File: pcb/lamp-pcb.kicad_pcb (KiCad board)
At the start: 2 copper layers, 105.4 x 91.4 mm, 41 parts, among them IC1 ATMEGA328P, IC2 LM1117, IC3 TLC5973, J1 5V_OUT, J2 LED_CARD_BOTTOM, M2 Val**, P1 7-12V_IN, P2 AVR_ISP, P3 SERIAL, P4 LEDSTACK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

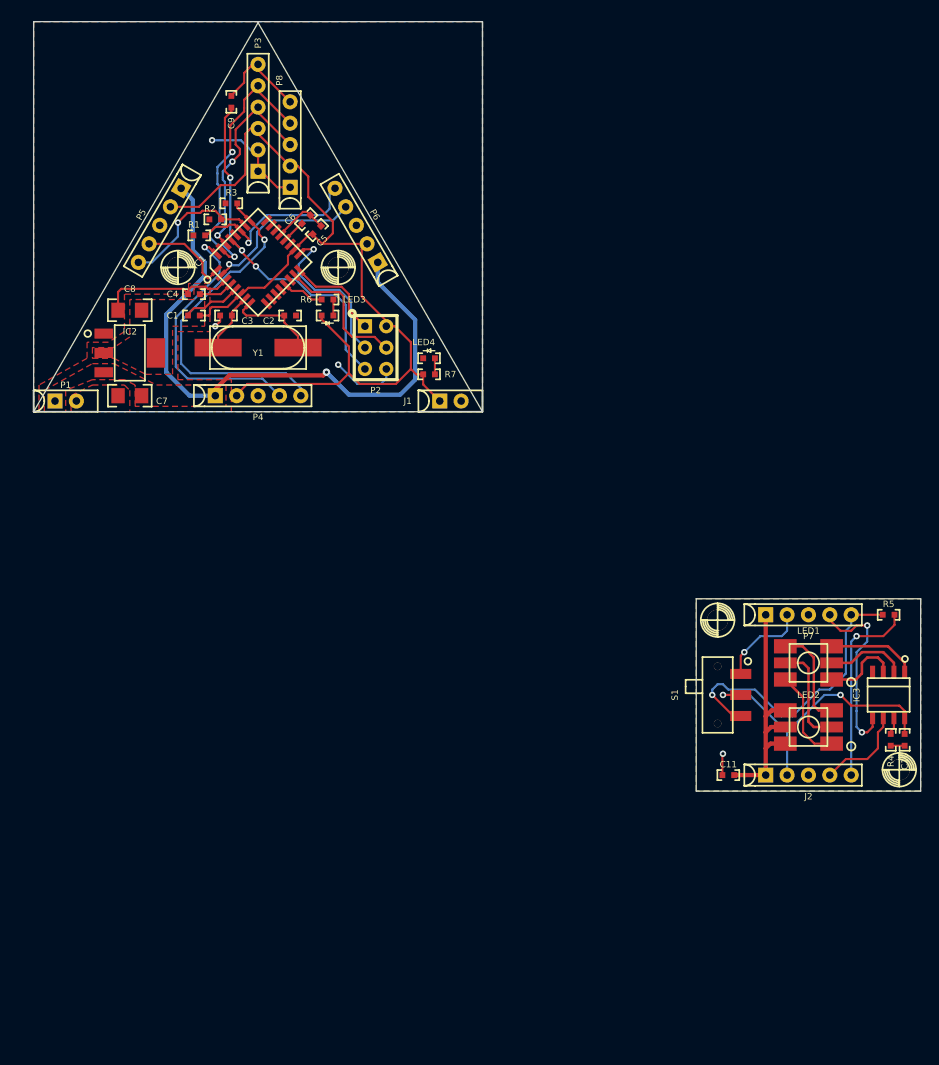
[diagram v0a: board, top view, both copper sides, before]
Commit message: silkscreen cleaned up. need to figure out how I actually want to panelize
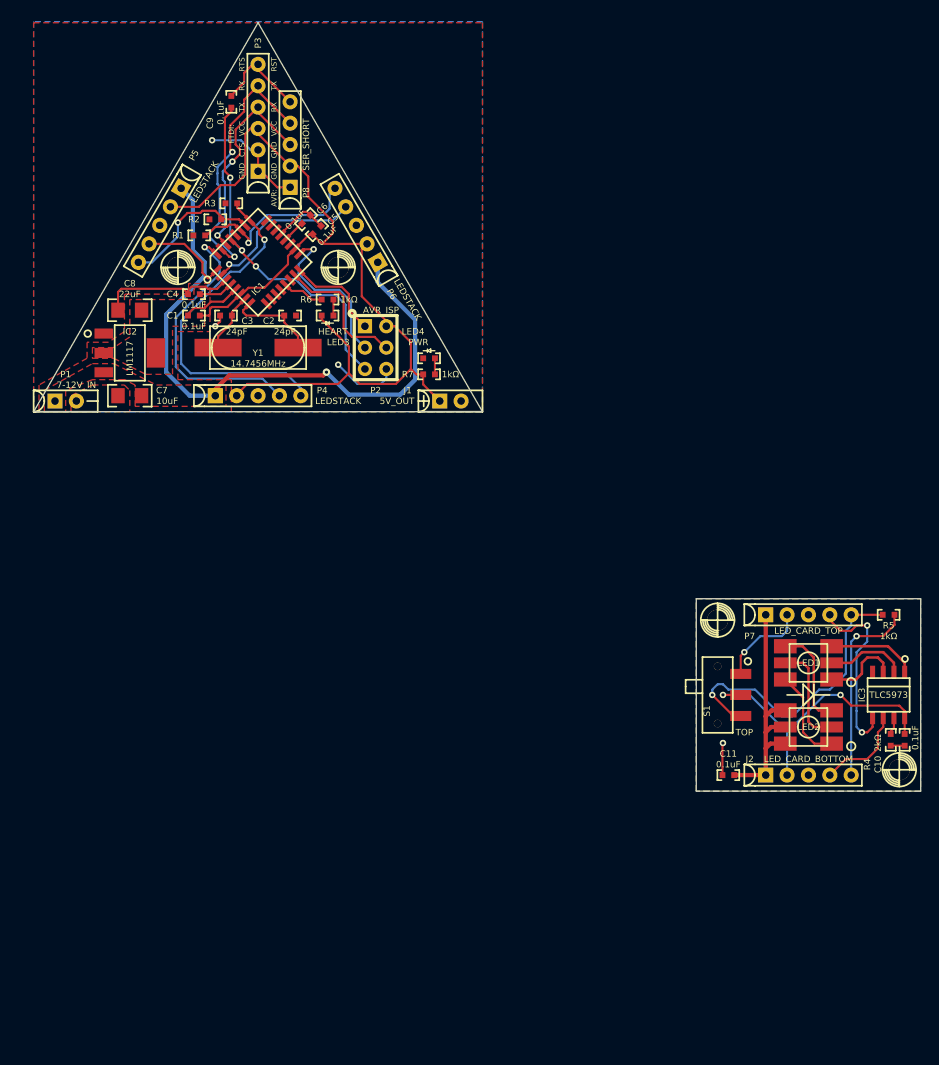
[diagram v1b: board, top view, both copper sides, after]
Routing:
- net /LED_GND: track 4.22 -> 5.49 mm
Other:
- board size 105.4 x 91.4 mm -> 105.4 x 91.3 mm
- board text added: "AVR:"
- board text added: "CTS"
- board text added: "FTDI:"
- board text added: "GND"
- board text added: "RST"
- board text added: "RTS"
- board text added: "RX"
- board text added: "TX"
- board text added: "VCC"

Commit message: i like this panelization layout
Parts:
- removed the C10 at (177.2, 141.2)
- removed the IC3 at (175.3, 135.9)
- added C10: 0.1uF, passive-smd:0603(1608m), F.Cu at (125.7, 171.7)
- added C10: 0.1uF, passive-smd:0603(1608m), F.Cu at (97.8, 171.7)
- added C10: 0.1uF, passive-smd:0603(1608m), F.Cu at (97.8, 146.3)
- added C10: 0.1uF, passive-smd:0603(1608m), F.Cu at (125.7, 146.3)
- added C10: 0.1uF, passive-smd:0603(1608m), F.Cu at (125.7, 120.9)
- added C10: 0.1uF, passive-smd:0603(1608m), F.Cu at (97.8, 120.9)
- added C11: 0.1uF, passive-smd:0603(1608m), F.Cu at (104.8, 175.9)
- added C11: 0.1uF, passive-smd:0603(1608m), F.Cu at (76.8, 175.9)
- added C11: 0.1uF, passive-smd:0603(1608m), F.Cu at (76.8, 150.5)
- added C11: 0.1uF, passive-smd:0603(1608m), F.Cu at (104.8, 150.5)
- added C11: 0.1uF, passive-smd:0603(1608m), F.Cu at (104.8, 125.1)
- added IC3: TLC5973, soic:SOIC8, F.Cu at (123.8, 166.4)
- added IC3: TLC5973, soic:SOIC8, F.Cu at (95.9, 166.4)
- added IC3: TLC5973, soic:SOIC8, F.Cu at (95.9, 141.0)
- added IC3: TLC5973, soic:SOIC8, F.Cu at (123.8, 141.0)
- added IC3: TLC5973, soic:SOIC8, F.Cu at (123.8, 115.6)
- added IC3: TLC5973, soic:SOIC8, F.Cu at (95.9, 115.6)
- added J2: LED_CARD_BOTTOM, sip:SIP5, F.Cu at (114.3, 175.9)
- added J2: LED_CARD_BOTTOM, sip:SIP5, F.Cu at (86.4, 175.9)
- added J2: LED_CARD_BOTTOM, sip:SIP5, F.Cu at (86.4, 150.5)
- added J2: LED_CARD_BOTTOM, sip:SIP5, F.Cu at (114.3, 150.5)
- added J2: LED_CARD_BOTTOM, sip:SIP5, F.Cu at (114.3, 125.1)
- added LED1: CREE-CLV6A-FKB, led:PLCC6-SM-RGB-LED, F.Cu at (114.3, 162.6)
- added LED1: CREE-CLV6A-FKB, led:PLCC6-SM-RGB-LED, F.Cu at (86.4, 162.6)
- added LED1: CREE-CLV6A-FKB, led:PLCC6-SM-RGB-LED, F.Cu at (86.4, 137.2)
- added LED1: CREE-CLV6A-FKB, led:PLCC6-SM-RGB-LED, F.Cu at (114.3, 137.2)
- added LED1: CREE-CLV6A-FKB, led:PLCC6-SM-RGB-LED, F.Cu at (114.3, 111.8)
- added LED2: CREE-CLV6A-FKB, led:PLCC6-SM-RGB-LED, F.Cu at (114.3, 170.2)
- added LED2: CREE-CLV6A-FKB, led:PLCC6-SM-RGB-LED, F.Cu at (86.4, 170.2)
- added LED2: CREE-CLV6A-FKB, led:PLCC6-SM-RGB-LED, F.Cu at (86.4, 144.8)
- added LED2: CREE-CLV6A-FKB, led:PLCC6-SM-RGB-LED, F.Cu at (114.3, 144.8)
- added LED2: CREE-CLV6A-FKB, led:PLCC6-SM-RGB-LED, F.Cu at (114.3, 119.4)
- added M2: Val**, asm:M2, F.Cu at (104.1, 157.5)
- added M2: Val**, asm:M2, F.Cu at (124.5, 124.5)
- added M2: Val**, asm:M2, F.Cu at (124.5, 175.3)
- added M2: Val**, asm:M2, F.Cu at (96.5, 175.3)
- added M2: Val**, asm:M2, F.Cu at (76.2, 157.5)
- added M2: Val**, asm:M2, F.Cu at (76.2, 132.1)
- added M2: Val**, asm:M2, F.Cu at (96.5, 149.9)
- added M2: Val**, asm:M2, F.Cu at (124.5, 149.9)
- added M2: Val**, asm:M2, F.Cu at (104.1, 132.1)
- added M2: Val**, asm:M2, F.Cu at (104.1, 106.7)
- added P7: LED_CARD_TOP, sip:SIP5, F.Cu at (114.3, 156.8)
- added P7: LED_CARD_TOP, sip:SIP5, F.Cu at (86.4, 156.8)
- added P7: LED_CARD_TOP, sip:SIP5, F.Cu at (86.4, 131.4)
- added P7: LED_CARD_TOP, sip:SIP5, F.Cu at (114.3, 131.4)
- added P7: LED_CARD_TOP, sip:SIP5, F.Cu at (114.3, 106.0)
- added R4: 2kΩ, passive-smd:0603(1608m), F.Cu at (124.1, 171.7)
- added R4: 2kΩ, passive-smd:0603(1608m), F.Cu at (96.1, 171.7)
- added R4: 2kΩ, passive-smd:0603(1608m), F.Cu at (96.1, 146.3)
- added R4: 2kΩ, passive-smd:0603(1608m), F.Cu at (124.1, 146.3)
- added R4: 2kΩ, passive-smd:0603(1608m), F.Cu at (124.1, 120.9)
- added R5: 1kΩ, passive-smd:0603(1608m), F.Cu at (123.8, 156.8)
- added R5: 1kΩ, passive-smd:0603(1608m), F.Cu at (95.9, 156.8)
- added R5: 1kΩ, passive-smd:0603(1608m), F.Cu at (95.9, 131.4)
- added R5: 1kΩ, passive-smd:0603(1608m), F.Cu at (123.8, 131.4)
- added R5: 1kΩ, passive-smd:0603(1608m), F.Cu at (123.8, 106.0)
- added S1: TOP, switch:CK-JS102011SAQN_sm-spdt-switch, F.Cu at (75.6, 166.4)
- added S1: TOP, switch:CK-JS102011SAQN_sm-spdt-switch, F.Cu at (75.6, 141.0)
- moved M2 82.5 mm to (96.5, 124.5)
- moved C11 81.9 mm to (76.8, 125.1)
- moved J2 81.9 mm to (86.4, 125.1)
- moved LED1 81.9 mm to (86.4, 111.8)
- moved LED2 81.9 mm to (86.4, 119.4)
- moved P7 81.9 mm to (86.4, 106.0)
- moved R4 81.9 mm to (96.1, 120.9)
- moved S1 81.9 mm to (75.6, 115.6)
- moved R5 81.9 mm to (95.9, 106.0)
- moved M2 81.3 mm to (76.2, 106.7)
- moved C1 0.64 mm to (92.7, 90.2)
- moved C2 0.64 mm to (104.1, 90.2)
- moved C3 0.64 mm to (96.5, 90.2)
- moved C4 0.64 mm to (92.7, 87.6)
- moved C6 0.64 mm to (106.0, 78.7)
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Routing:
- net /VLOG: track 36.0 -> 215.9 mm, vias 2 -> 12
- net /SENSE_TOP: track 35.9 -> 215.2 mm, vias 1 -> 6
- net /VLED: track 30.6 -> 183.4 mm
- net /SENSE_BOT: track 23.0 -> 138.2 mm, vias 1 -> 6
- net /LED_SER_OUT: track 22.0 -> 127.9 mm, vias 2 -> 12
- net Net-(LED1-Pad5): track 12.4 -> 74.3 mm
- net Net-(LED1-Pad4): track 12.0 -> 72.0 mm
- net Net-(LED1-Pad6): track 11.1 -> 66.6 mm
- net /LED_SER_IN: track 10.9 -> 65.7 mm
- net /VLOG_TOP: track 10.8 -> 64.8 mm, vias 1 -> 6
- net /RED: track 10.6 -> 63.6 mm
- net /GRN: track 9.57 -> 57.4 mm
- net /BLU: track 9.34 -> 56.0 mm
- net /LED_GND: track 5.49 -> 32.9 mm, vias 1 -> 6
- net Net-(IC3-Pad7): track 2.09 -> 12.6 mm
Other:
- board size 105.4 x 91.3 mm -> 53.3 x 122.4 mm

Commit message: full panel
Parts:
- added MOUSEBITE: VAL**, asm:MOUSEBITE, F.Cu at (113.5, 128.3)
- added MOUSEBITE: VAL**, asm:MOUSEBITE, F.Cu at (114.3, 153.7)
- added MOUSEBITE: VAL**, asm:MOUSEBITE, F.Cu at (115.1, 153.7)
- added MOUSEBITE: VAL**, asm:MOUSEBITE, F.Cu at (113.5, 153.7)
- added MOUSEBITE: VAL**, asm:MOUSEBITE, F.Cu at (85.6, 102.9)
- added MOUSEBITE: VAL**, asm:MOUSEBITE, F.Cu at (86.4, 102.9)
- added MOUSEBITE: VAL**, asm:MOUSEBITE, F.Cu at (87.1, 102.9)
- added MOUSEBITE: VAL**, asm:MOUSEBITE, F.Cu at (115.1, 102.9)
- added MOUSEBITE: VAL**, asm:MOUSEBITE, F.Cu at (114.3, 102.9)
- added MOUSEBITE: VAL**, asm:MOUSEBITE, F.Cu at (113.5, 102.9)
- added MOUSEBITE: VAL**, asm:MOUSEBITE, F.Cu at (100.3, 115.6)
- added MOUSEBITE: VAL**, asm:MOUSEBITE, F.Cu at (115.1, 128.3)
- added MOUSEBITE: VAL**, asm:MOUSEBITE, F.Cu at (100.3, 114.8)
- added MOUSEBITE: VAL**, asm:MOUSEBITE, F.Cu at (100.3, 116.3)
- added MOUSEBITE: VAL**, asm:MOUSEBITE, F.Cu at (100.3, 140.2)
- added MOUSEBITE: VAL**, asm:MOUSEBITE, F.Cu at (100.3, 141.0)
- added MOUSEBITE: VAL**, asm:MOUSEBITE, F.Cu at (100.3, 141.7)
- added MOUSEBITE: VAL**, asm:MOUSEBITE, F.Cu at (100.3, 165.6)
- added MOUSEBITE: VAL**, asm:MOUSEBITE, F.Cu at (100.3, 166.4)
- added MOUSEBITE: VAL**, asm:MOUSEBITE, F.Cu at (100.3, 167.1)
- added MOUSEBITE: VAL**, asm:MOUSEBITE, F.Cu at (114.3, 128.3)
- added MOUSEBITE: VAL**, asm:MOUSEBITE, F.Cu at (86.4, 128.3)
- added MOUSEBITE: VAL**, asm:MOUSEBITE, F.Cu at (87.1, 128.3)
- added MOUSEBITE: VAL**, asm:MOUSEBITE, F.Cu at (85.6, 128.3)
- added MOUSEBITE: VAL**, asm:MOUSEBITE, F.Cu at (85.6, 153.7)
- added MOUSEBITE: VAL**, asm:MOUSEBITE, F.Cu at (87.1, 153.7)
- added MOUSEBITE: VAL**, asm:MOUSEBITE, F.Cu at (86.4, 153.7)
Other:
- outline, holes or cut-outs redrawn

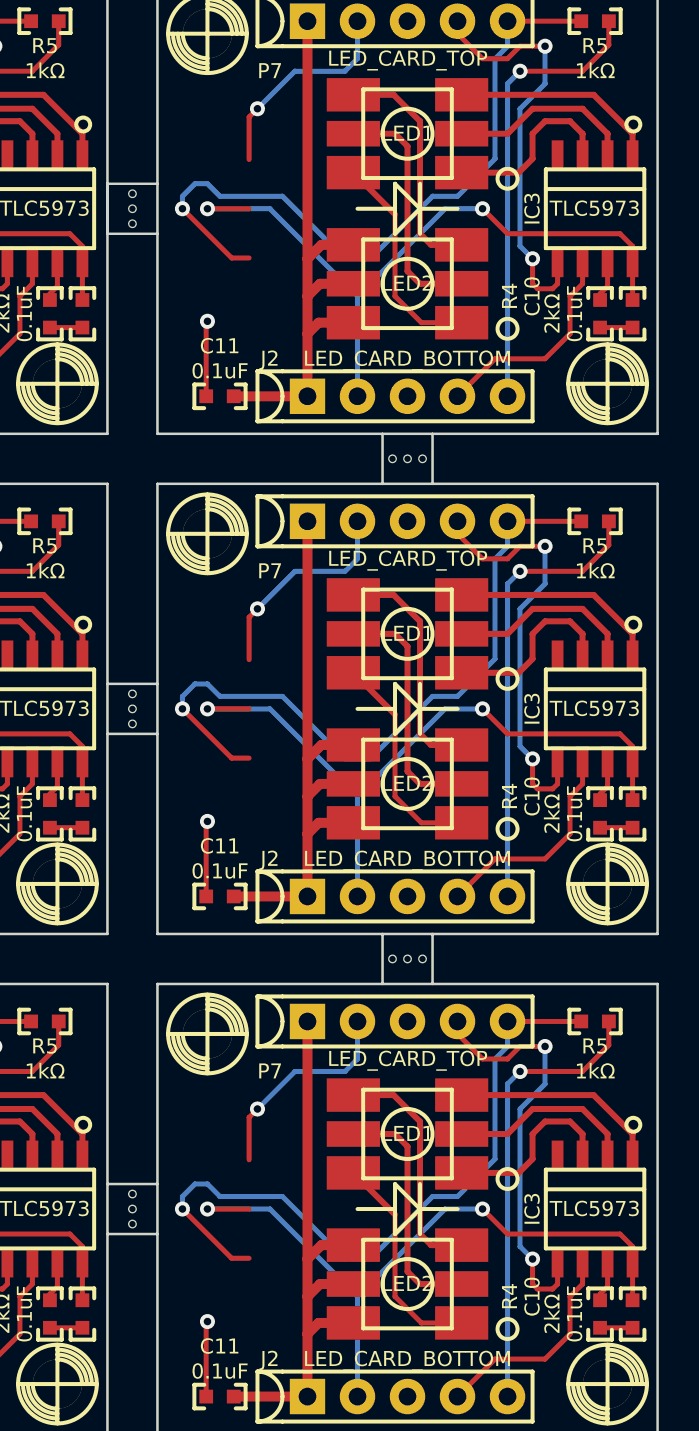
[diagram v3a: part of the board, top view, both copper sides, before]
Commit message: jk roflcopter. panel is now correct
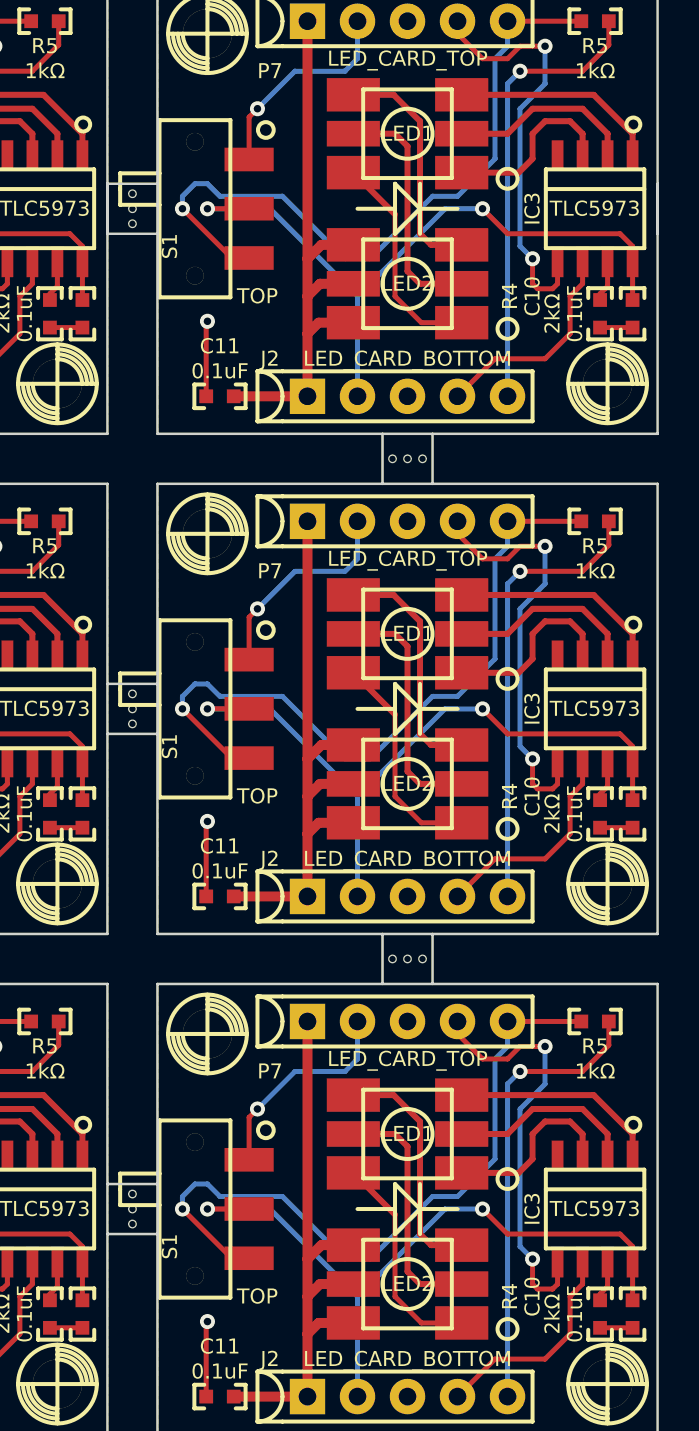
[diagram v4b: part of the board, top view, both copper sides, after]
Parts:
- added S1: TOP, switch:CK-JS102011SAQN_sm-spdt-switch, F.Cu at (103.5, 115.6)
- added S1: TOP, switch:CK-JS102011SAQN_sm-spdt-switch, F.Cu at (103.5, 141.0)
- added S1: TOP, switch:CK-JS102011SAQN_sm-spdt-switch, F.Cu at (103.5, 166.4)
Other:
- outline, holes or cut-outs redrawn
